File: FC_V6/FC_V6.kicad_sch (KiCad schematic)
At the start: 0 parts

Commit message: Sheets First Cut
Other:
- added sheet Connectors (connectors.kicad_sch)
- added sheet Load Switches (load_switches.kicad_sch)
- added sheet Onboard Sensors (sensors.kicad_sch)
- added sheet Peripherals (untitled.kicad_sch)
- added sheet Power Inhibits (power_inhibits.kicad_sch)
- added sheet Power Management (power.kicad_sch)
- added sheet Rad Tolerant Watchdog (watchdog.kicad_sch)
- added sheet Radios (radios.kicad_sch)

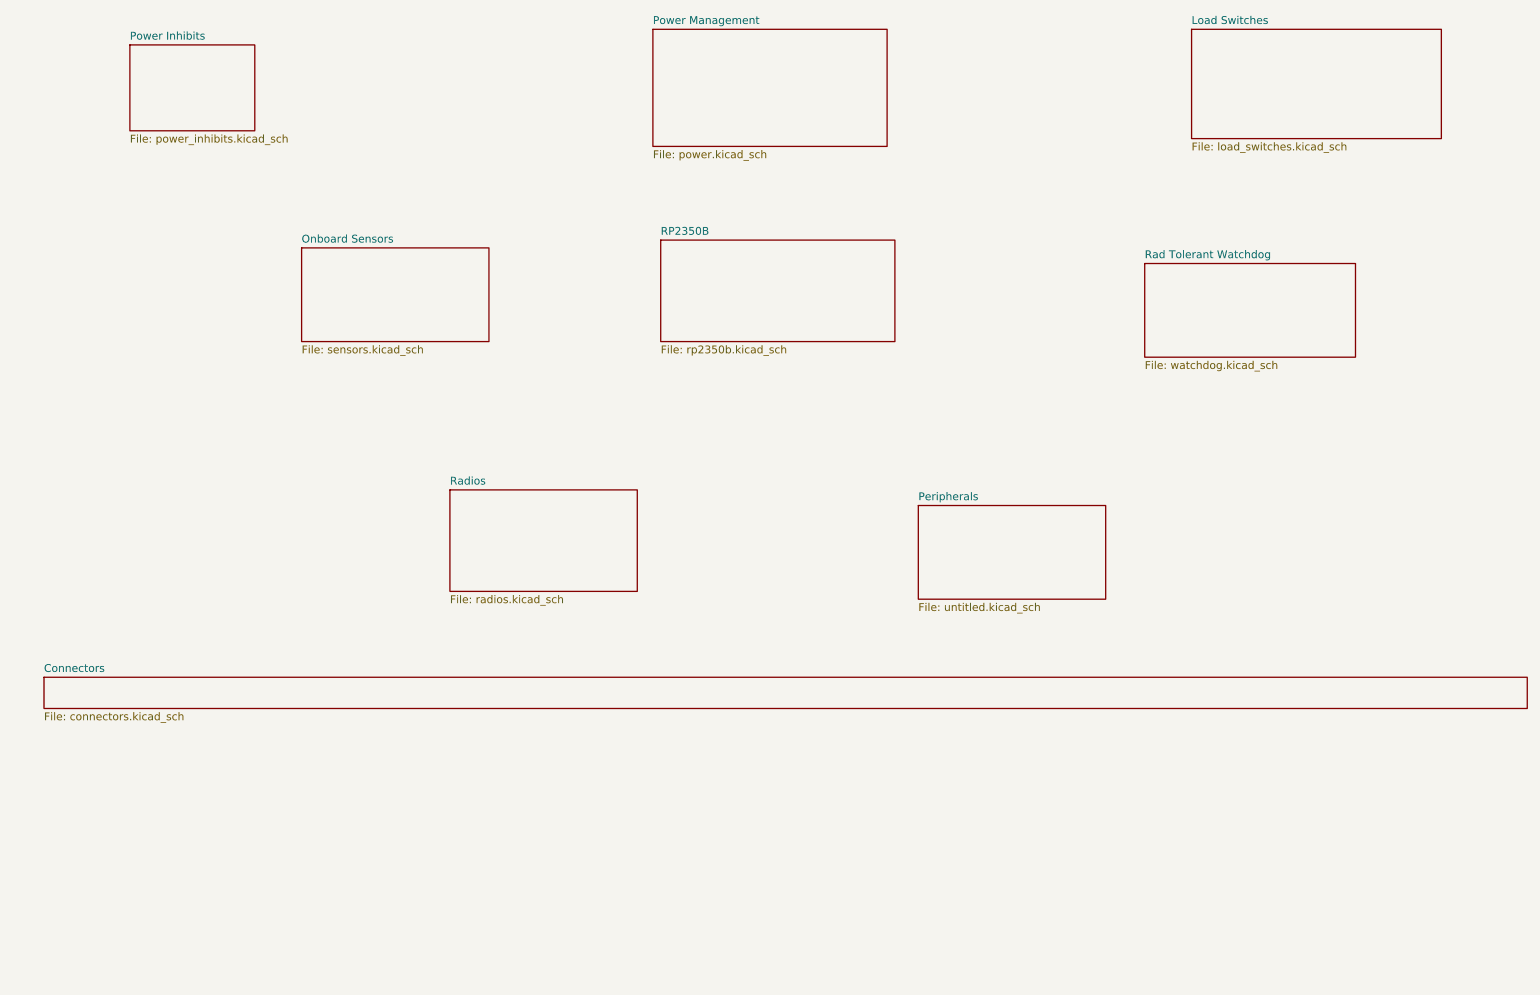
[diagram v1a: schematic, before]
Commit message: Updated Flash Memory Schematic
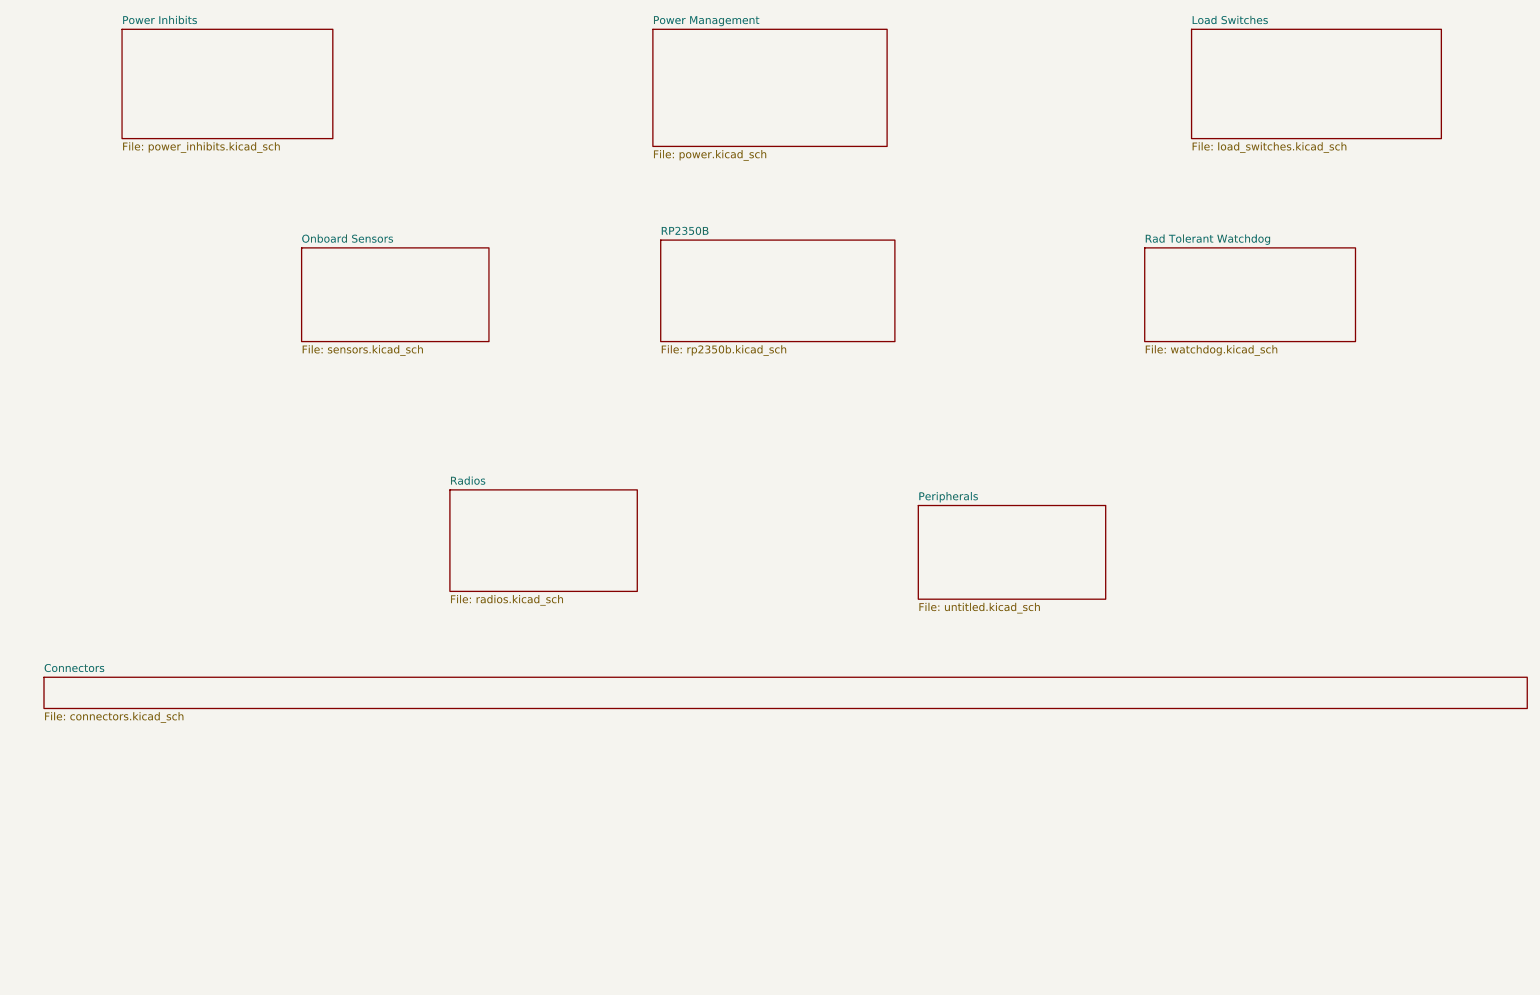
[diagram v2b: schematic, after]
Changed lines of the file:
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@@
 	)
 	(sheet
-		(at 207.01 76.2)
+		(at 207.01 73.66)
 		(size 34.29 15.24)
 		(exclude_from_sim no)
@@
 		)
 		(property "Sheetname" "Rad Tolerant Watchdog"
-			(at 207.01 75.4884 0)
+			(at 207.01 72.9484 0)
 			(effects
 				(font
@@
 		)
 		(property "Sheetfile" "watchdog.kicad_sch"
-			(at 207.01 92.0246 0)
+			(at 207.01 89.4846 0)
 			(effects
 				(font
@@
 	)
 	(sheet
-		(at 41.91 40.64)
-		(size 20.32 13.97)
+		(at 40.64 38.1)
+		(size 34.29 17.78)
 		(exclude_from_sim no)
 		(in_bom yes)
@@
 		)
 		(property "Sheetname" "Power Inhibits"
-			(at 41.91 39.9284 0)
+			(at 40.64 37.3884 0)
 			(effects
 				(font
@@
 		)
 		(property "Sheetfile" "power_inhibits.kicad_sch"
-			(at 41.91 55.1946 0)
+			(at 40.64 56.4646 0)
 			(effects
 				(font

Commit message: Delete RP2350B
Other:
- removed sheet RP2350B
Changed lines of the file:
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@@
 (kicad_sch
-	(version 20250114)
+	(version 20260306)
 	(generator "eeschema")
-	(generator_version "9.0")
+	(generator_version "10.0")
 	(paper "A4")
 	(sheet
@@
 		)
 		(fill
-			(color 0 0 0 0.0000)
+			(color 0 0 0 0)
 		)
 		(property "Sheetname" "Onboard Sensors"
 			(at 69.85 72.9484 0)
+			(show_name no)
+			(do_not_autoplace no)
 			(effects
 				(font
@@
 		(property "Sheetfile" "sensors.kicad_sch"
 			(at 69.85 89.4846 0)
+			(show_name no)
+			(do_not_autoplace no)
 			(effects
 				(font
@@
 		)
 		(fill
-			(color 0 0 0 0.0000)
+			(color 0 0 0 0)
 		)
 		(property "Sheetname" "Load Switches"
 			(at 214.63 37.3884 0)
+			(show_name no)
+			(do_not_autoplace no)
 			(effects
 				(font
@@
 		(property "Sheetfile" "load_switches.kicad_sch"
 			(at 214.63 56.4646 0)
+			(show_name no)
+			(do_not_autoplace no)
 			(effects
 				(font
@@
 		)
 		(fill
-			(color 0 0 0 0.0000)
+			(color 0 0 0 0)
 		)
 		(property "Sheetname" "Rad Tolerant Watchdog"
 			(at 207.01 72.9484 0)
+			(show_name no)
+			(do_not_autoplace no)
 			(effects
 				(font
@@
 		(property "Sheetfile" "watchdog.kicad_sch"
 			(at 207.01 89.4846 0)
+			(show_name no)
+			(do_not_autoplace no)
 			(effects
 				(font
@@
 		)
 		(fill
-			(color 0 0 0 0.0000)
+			(color 0 0 0 0)
 		)
 		(property "Sheetname" "Power Inhibits"
 			(at 40.64 37.3884 0)
+			(show_name no)
+			(do_not_autoplace no)
 			(effects
 				(font
@@
 		(property "Sheetfile" "power_inhibits.kicad_sch"
 			(at 40.64 56.4646 0)
+			(show_name no)
+			(do_not_autoplace no)
 			(effects
 				(font
@@
 		)
 		(fill
-			(color 0 0 0 0.0000)
+			(color 0 0 0 0)
 		)
 		(property "Sheetname" "Radios"
 			(at 93.98 112.3184 0)
+			(show_name no)
+			(do_not_autoplace no)
 			(effects
 				(font
@@
 		(property "Sheetfile" "radios.kicad_sch"
 			(at 93.98 130.1246 0)
+			(show_name no)
+			(do_not_autoplace no)
 			(effects
 				(font
@@
 				(path "/f080da98-69f4-43da-b75c-192226370aa3"
 					(page "7")
-				)
-			)
-		)
-	)
-	(sheet
-		(at 128.27 72.39)
-		(size 38.1 16.51)
-		(exclude_from_sim no)
-		(in_bom yes)
-		(on_board yes)
-		(dnp no)
-		(fields_autoplaced yes)
-		(stroke
-			(width 0.1524)
-			(type solid)
-		)
-		(fill
-			(color 0 0 0 0.0000)
-		)
-		(property "Sheetname" "RP2350B"
-			(at 128.27 71.6784 0)
-			(effects
-				(font
-					(size 1.27 1.27)
-				)
-				(justify left bottom)
-			)
-		)
-		(property "Sheetfile" "rp2350b.kicad_sch"
-			(at 128.27 89.4846 0)
-			(effects
-				(font
-					(size 1.27 1.27)
-				)
-				(justify left top)
-			)
-		)
-		(instances
-			(project "FC_V6"
-				(path "/f080da98-69f4-43da-b75c-192226370aa3"
-					(page "2")
 				)
 			)
@@
 		)
 		(fill
-			(color 0 0 0 0.0000)
+			(color 0 0 0 0)
 		)
 		(property "Sheetname" "Connectors"
 			(at 27.94 142.7984 0)
+			(show_name no)
+			(do_not_autoplace no)
 			(effects
 				(font
@@
 		(property "Sheetfile" "connectors.kicad_sch"
 			(at 27.94 149.1746 0)
+			(show_name no)
+			(do_not_autoplace no)
 			(effects
 				(font
@@
 		)
 		(fill
-			(color 0 0 0 0.0000)
+			(color 0 0 0 0)
 		)
 		(property "Sheetname" "Peripherals"
 			(at 170.18 114.8584 0)
+			(show_name no)
+			(do_not_autoplace no)
 			(effects
 				(font
@@
 		(property "Sheetfile" "untitled.kicad_sch"
 			(at 170.18 131.3946 0)
+			(show_name no)
+			(do_not_autoplace no)
 			(effects
 				(font
@@
 		)
 		(fill
-			(color 0 0 0 0.0000)
+			(color 0 0 0 0)
 		)
 		(property "Sheetname" "Power Management"
 			(at 127 37.3884 0)
+			(show_name no)
+			(do_not_autoplace no)
 			(effects
 				(font
@@
 		(property "Sheetfile" "power.kicad_sch"
 			(at 127 57.7346 0)
-			(effects
-				(font
+			(show_name no)
+			(do_not_autoplace no)
+			(effects
+				(font

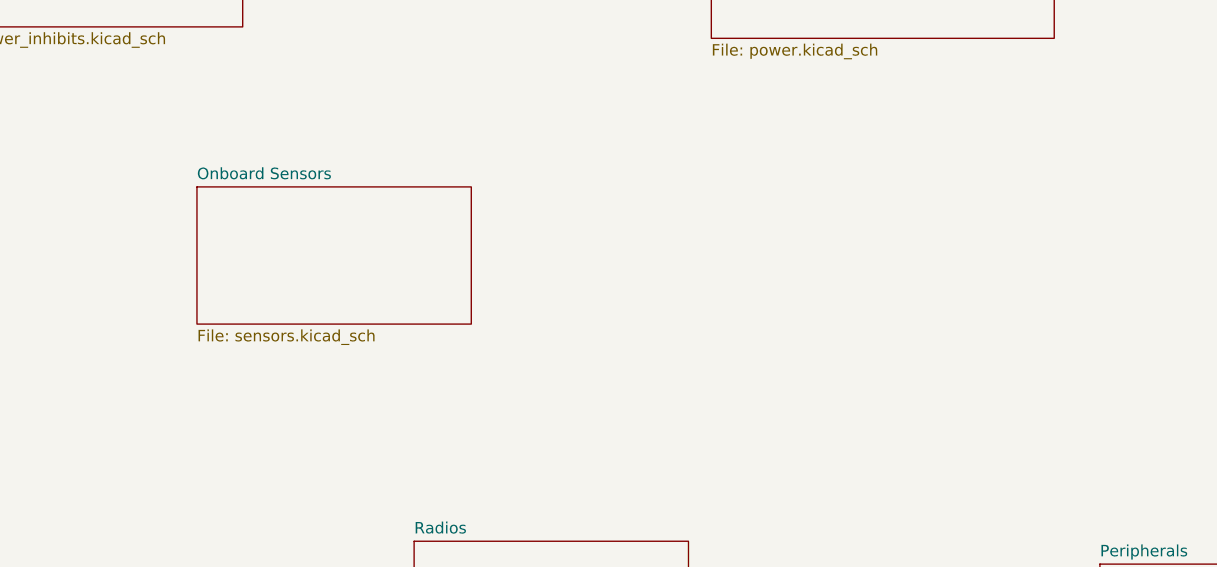
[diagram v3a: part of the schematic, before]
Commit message: Create STM32 MCU Sheet
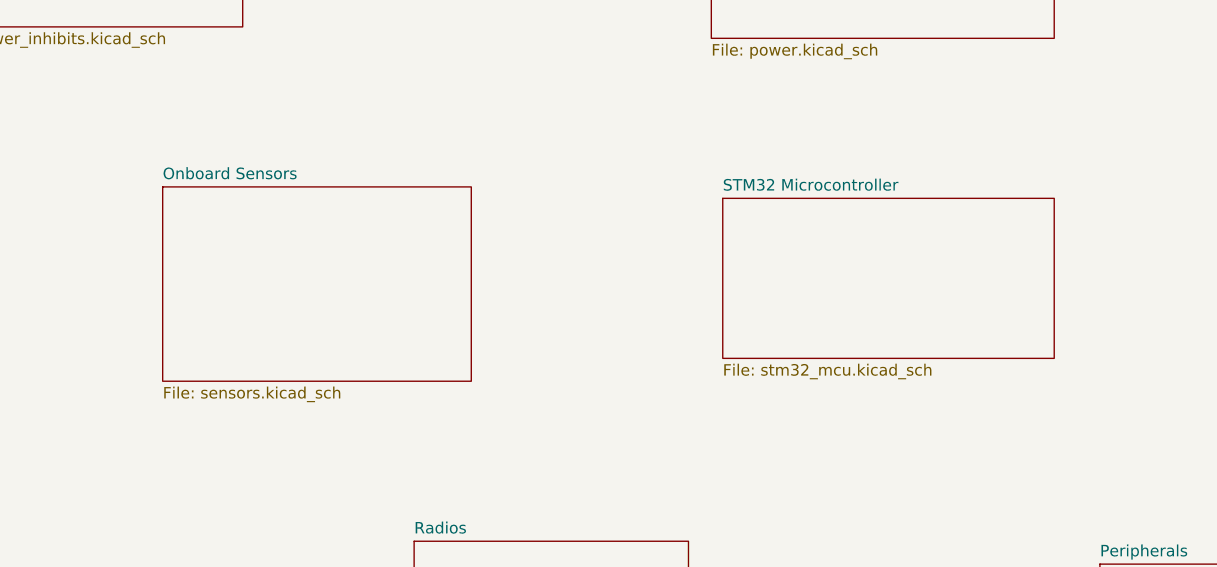
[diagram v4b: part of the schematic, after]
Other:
- added sheet STM32 Microcontroller (stm32_mcu.kicad_sch)
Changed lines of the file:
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@@
 	(paper "A4")
 	(sheet
-		(at 69.85 73.66)
-		(size 30.48 15.24)
+		(at 66.04 73.66)
+		(size 34.29 21.59)
 		(exclude_from_sim no)
 		(in_bom yes)
@@
 		)
 		(property "Sheetname" "Onboard Sensors"
-			(at 69.85 72.9484 0)
+			(at 66.04 72.9484 0)
 			(show_name no)
 			(do_not_autoplace no)
@@
 		)
 		(property "Sheetfile" "sensors.kicad_sch"
-			(at 69.85 89.4846 0)
+			(at 66.04 95.8346 0)
 			(show_name no)
 			(do_not_autoplace no)
@@
 				)
 			)
+		)
+	)
+	(sheet
+		(at 128.27 74.93)
+		(size 36.83 17.78)
+		(exclude_from_sim no)
+		(in_bom yes)
+		(on_board yes)
+		(dnp no)
+		(fields_autoplaced yes)
+		(stroke
+			(width 0.1524)
+			(type solid)
+		)
+		(fill
+			(color 0 0 0 0)
+		)
+		(property "Sheetname" "STM32 Microcontroller"
+			(at 128.27 74.2184 0)
+			(show_name no)
+			(do_not_autoplace no)
+			(effects
+				(font
+					(size 1.27 1.27)
+				)
+				(justify left bottom)
+			)
+		)
+		(property "Sheetfile" "stm32_mcu.kicad_sch"
+			(at 128.27 93.2946 0)
+			(show_name no)
+			(do_not_autoplace no)
+			(effects
+				(font
+					(size 1.27 1.27)
+				)
+				(justify left top)
+			)
+		)
+		(instances
+			(project "FC_V6"
+				(path "/f080da98-69f4-43da-b75c-192226370aa3"
+					(page "2")
+				)
+			)

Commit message: Did Some Block Diagram Work
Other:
- added sheet Power System Block Diagram (power_block_diagram.kicad_sch)
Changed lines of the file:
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@@
+		)
+	)
+	(sheet
+		(at 22.86 177.8)
+		(size 25.4 12.7)
+		(exclude_from_sim no)
+		(in_bom yes)
+		(on_board yes)
+		(dnp no)
+		(fields_autoplaced yes)
+		(stroke
+			(width 0.1524)
+			(type solid)
+		)
+		(fill
+			(color 255 95 45 1)
+		)
+		(property "Sheetname" "Power System Block Diagram"
+			(at 22.86 177.0884 0)
+			(show_name no)
+			(do_not_autoplace no)
+			(effects
+				(font
+					(size 1.27 1.27)
+				)
+				(justify left bottom)
+			)
+		)
+		(property "Sheetfile" "power_block_diagram.kicad_sch"
+			(at 22.86 191.0846 0)
+			(show_name no)
+			(do_not_autoplace no)
+			(effects
+				(font
+					(size 1.27 1.27)
+				)
+				(justify left top)
+			)
+		)
+		(instances
+			(project "FC_V6"
+				(path "/f080da98-69f4-43da-b75c-192226370aa3"
+					(page "11")
+				)
+			)
 		)
 	)
